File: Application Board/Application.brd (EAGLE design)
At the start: 52.8 x 68.6 mm, 53 parts, among them Q1 DMP2012SN-7, T1 FDN340P, T2 AP1117_LIN_REG, U1 LM3409HV'LM3409HV'

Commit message: Cleaned up some of the traces
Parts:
- moved U$4 1.52 mm to (49.5, 58.2)
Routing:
- net GND: track 14.1 -> 33.1 mm, vias 45 -> 51
- net +3V3: track 153.2 -> 167.8 mm
- net N$58: track 29.0 -> 27.0 mm
- net N$57: track 3.15 -> 4.87 mm
- net L1: track 9.56 -> 11.1 mm
- net N$24: track 1.94 -> 3.49 mm
- net N$1: track 1.94 -> 3.49 mm
- net N$5: track 4.77 -> 5.30 mm

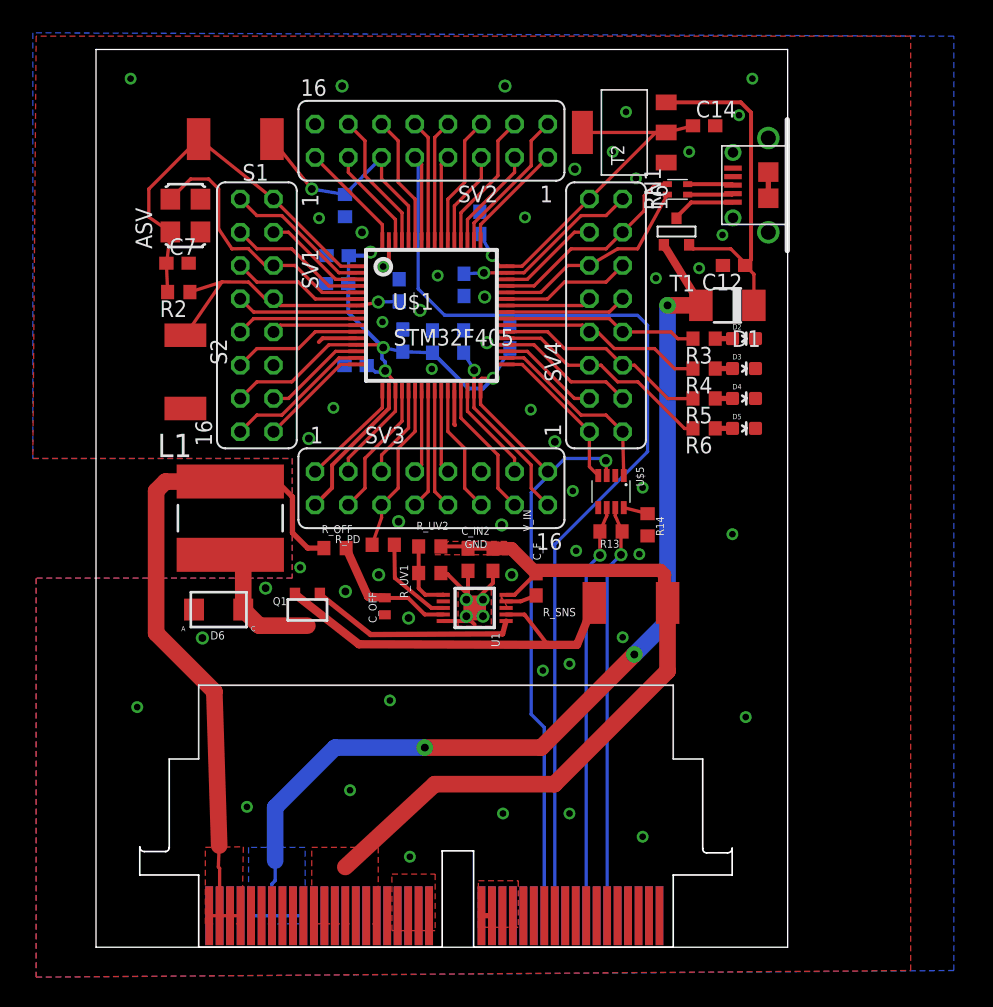
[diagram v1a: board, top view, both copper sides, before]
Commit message: Added The U Type +3V3 Wire
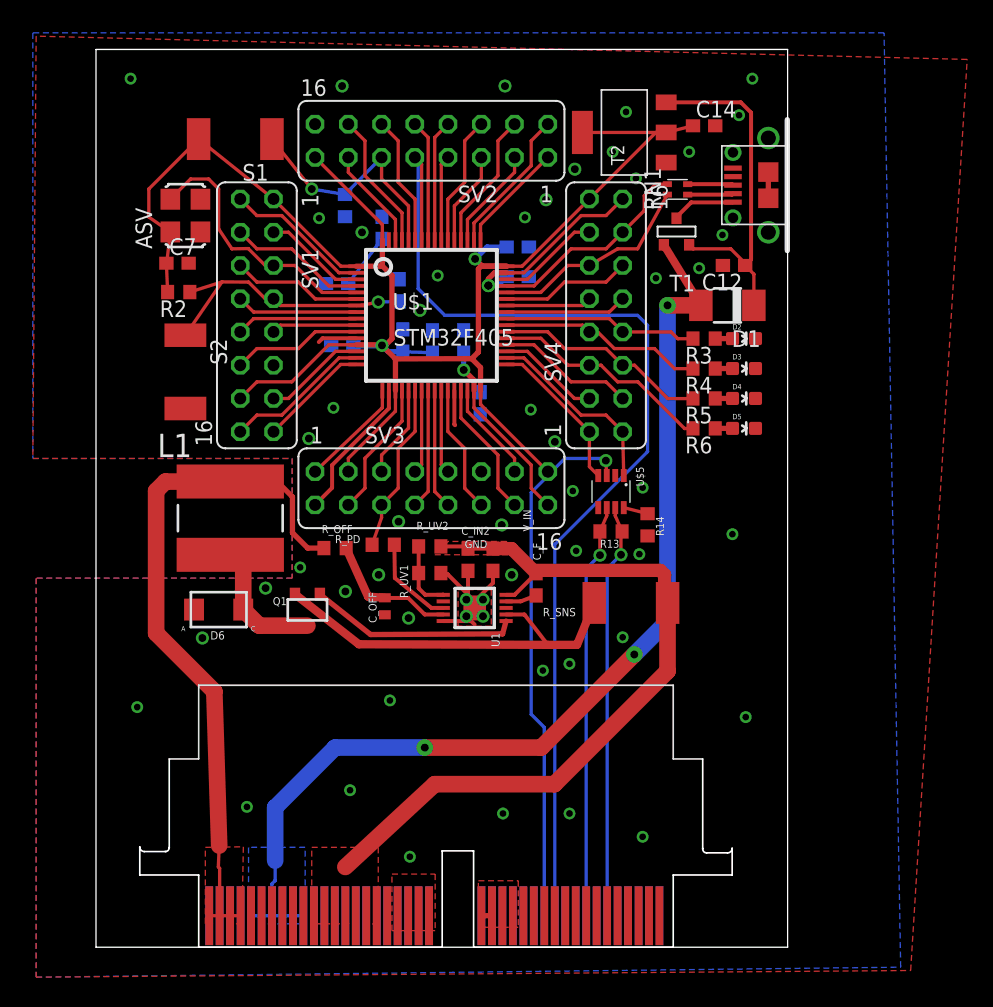
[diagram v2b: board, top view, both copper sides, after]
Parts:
- moved C4 5.52 mm to (26.0, 41.6), turned to 270 degrees
- moved C2 4.15 mm to (28.9, 51.2), turned to 180 degrees
- moved C6 3.99 mm to (18.5, 54.9), turned to 90 degrees
- moved C5 3.44 mm to (28.9, 53.5), turned to 180 degrees
- moved C3 1.83 mm to (15.5, 46.0)
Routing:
- net +3V3: track 167.8 -> 181.4 mm, vias 6 -> 3
- net GND: track 33.1 -> 30.9 mm, vias 51 -> 46
- net VCAP_2: track 14.5 -> 15.0 mm

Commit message: Update 1/15/16 4:50pm
Added Temp_Sens Pullup Resistor, connected remaining air wires, modified
path of a few lines
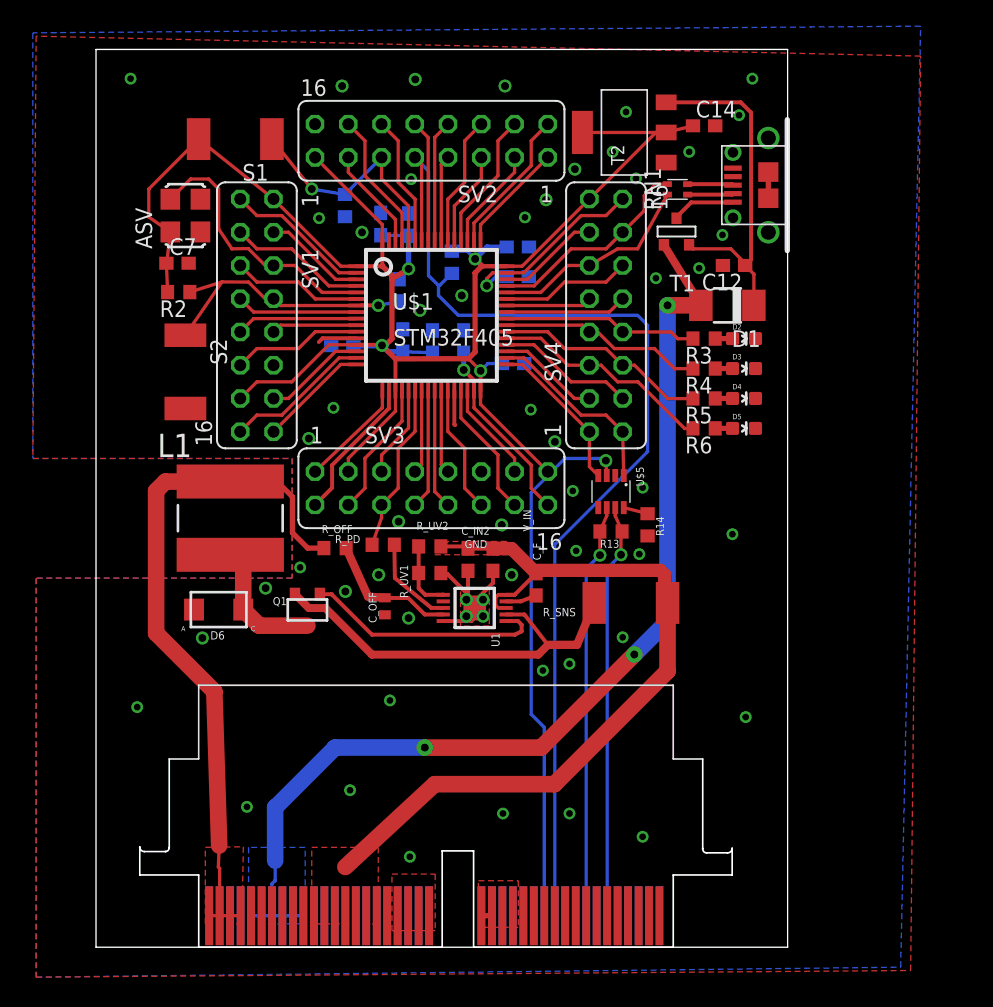
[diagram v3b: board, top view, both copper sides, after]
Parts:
- added R7: 4.7K, rcl:R0603
- R_OFF: value 7870 -> 7.87K
- R_PD: value 10000 -> 10K
- R_UV1: value 22600 -> 22.6K
- R_UV2: value 13700 -> 13.7K
- moved C8 5.63 mm to (18.4, 55.2), turned to 90 degrees
- moved C4 3.94 mm to (28.6, 44.6), turned to 180 degrees
- moved C6 2.05 mm to (20.6, 55.2)
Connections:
- net +3V3: now also R7.2
- net TEMP_SENS: now also R7.1
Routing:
- net +3V3: track 181.4 -> 187.4 mm, vias 3 -> 5
- net N$10: track 16.1 -> 18.6 mm
- net +12V: track 59.7 -> 62.1 mm
- net TEMP_SENS: track 83.4 -> 84.5 mm
- net N$8: track 30.7 -> 31.6 mm
- net GND: track 30.9 -> 30.8 mm, vias 46 -> 48

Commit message: Fixed some DLC Errors
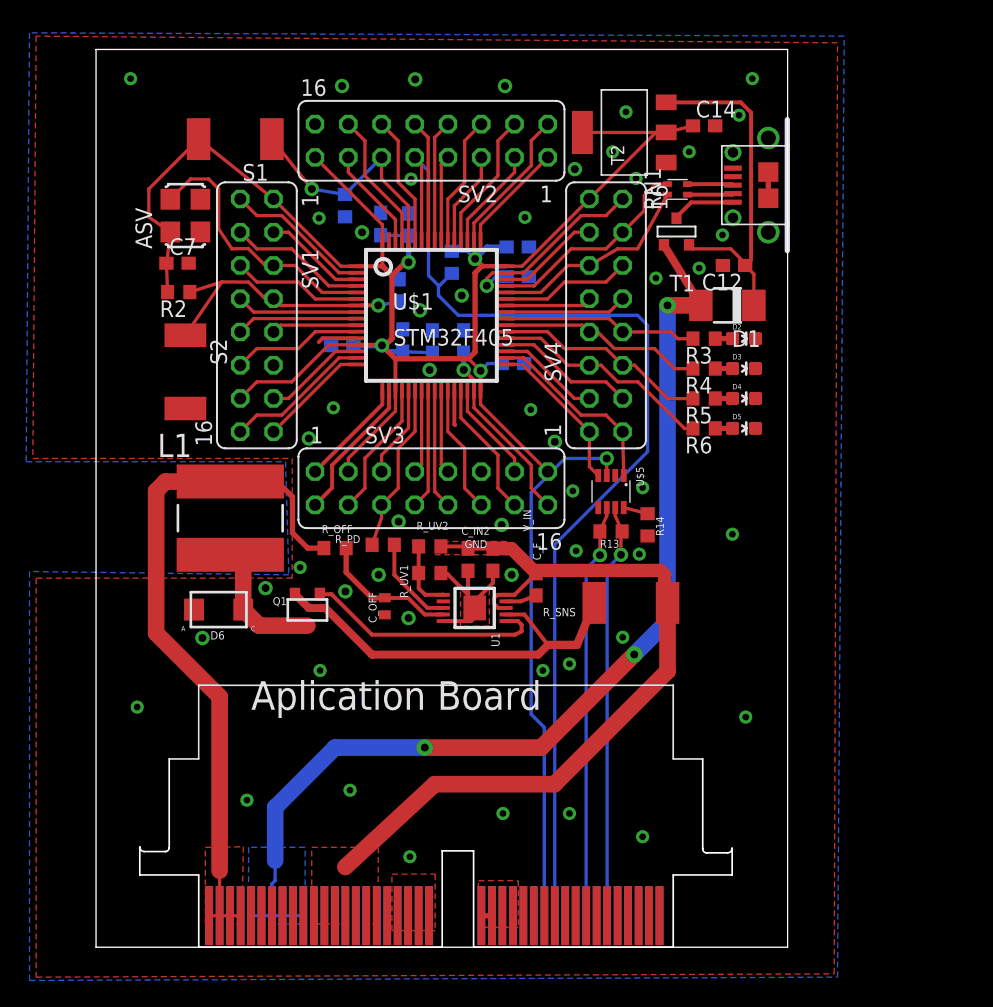
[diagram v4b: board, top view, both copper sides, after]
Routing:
- net CAM_LEDV: track 53.6 -> 55.6 mm
- net GND: track 30.8 -> 29.6 mm, vias 48 -> 44
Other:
- board text added: "Aplication Board"
